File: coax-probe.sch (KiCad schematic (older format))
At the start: 28 parts, among them J1 Conn_01x02, J2 Conn_Coaxial, J3 Conn_01x02, J4 Conn_01x03, J5 Conn_Coaxial, J6 Conn_01x03, U1 THS3001, U2 INA128, U3 THS3001

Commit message: use dual-supply for differential amp buffer
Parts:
- added C8: 100nF, Capacitor_SMD:C_0402_1005Metric, symbol Device:C_Small
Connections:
- wire segments 86 -> 91
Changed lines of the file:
@@
 	6100 5450 5900 5450
-$Comp
-L power:GND #PWR010
-U 1 1 606A7C58
-P 5650 5050
-F 0 "#PWR010" H 5650 4800 50  0001 C CNN
-F 1 "GND" H 5650 4900 50  0000 C CNN
-F 2 "" H 5650 5050 50  0001 C CNN
-F 3 "" H 5650 5050 50  0001 C CNN
-	1    5650 5050
-	1    0    0    -1
-$EndComp
 $Comp
 L power:VCC #PWR09
@@
 	1    0    0    -1
 $EndComp
+$Comp
+L power:VSS #PWR010
+U 1 1 6077A074
+P 6300 5350
+F 0 "#PWR010" H 6300 5200 50  0001 C CNN
+F 1 "VSS" H 6300 5500 50  0000 C CNN
+F 2 "" H 6300 5350 50  0001 C CNN
+F 3 "" H 6300 5350 50  0001 C CNN
+	1    6300 5350
+	-1   0    0    1
+$EndComp
+$Comp
+L power:GND #PWR018
+U 1 1 6077A07A
+P 6500 5350
+F 0 "#PWR018" H 6500 5100 50  0001 C CNN
+F 1 "GND" H 6500 5200 50  0000 C CNN
+F 2 "" H 6500 5350 50  0001 C CNN
+F 3 "" H 6500 5350 50  0001 C CNN
+	1    6500 5350
+	1    0    0    -1
+$EndComp
+Wire Wire Line
+	6500 5150 6500 5100
+Wire Wire Line
+	6500 5100 6300 5100
+$Comp
+L Device:C_Small C8
+U 1 1 6077A082
+P 6500 5250
+F 0 "C8" H 6592 5296 50  0000 L CNN
+F 1 "100nF" H 6592 5205 50  0000 L CNN
+F 2 "Capacitor_SMD:C_0402_1005Metric" H 6538 5100 50  0001 C CNN
+F 3 "~" H 6500 5250 50  0001 C CNN
+	1    6500 5250
+	1    0    0    -1
+$EndComp
+Wire Wire Line
+	6300 5350 6300 5100
+Wire Wire Line
+	5650 5050 5650 5100
+Wire Wire Line
+	5650 5100 6300 5100
+Connection ~ 6300 5100
 $EndSCHEMATC

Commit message: Improvements, layout
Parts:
- removed C2, C7: 10uF, Capacitor_SMD:C_0603_1608Metric, symbol Device:C
- removed C4, C8: 100nF, Capacitor_SMD:C_0402_1005Metric, symbol Device:C_Small
- removed D1, D2: SM4007PL, Diode_SMD:D_SOD-123F, symbol Device:D_ALT
- removed J3: Conn_01x02, Connector_PinHeader_2.54mm:PinHeader_1x02_P2.54mm_Vertical, symbol Connector_Generic:Conn_01x02
- removed U1, U3: THS3001, Package_SO:SOIC-8_3.9x4.9mm_P1.27mm, symbol Amplifier_Operational:LMH6609MA
- added C10, C11: 10uF, Capacitor_SMD:C_0603_1608Metric, symbol Device:C
- added C13, C9: 100nF, Capacitor_SMD:C_0402_1005Metric, symbol Device:C_Small
- added J3: Conn_01x03, Connector_PinHeader_2.54mm:PinHeader_1x03_P2.54mm_Vertical, symbol Connector_Generic:Conn_01x03
- added R11: 0, Resistor_SMD:R_0603_1608Metric, symbol Device:R_US
- added R12: -, Resistor_SMD:R_0603_1608Metric, symbol Device:R_US
- added U1, U3: OPA690, Package_TO_SOT_SMD:TSOT-23-6, symbol Amplifier_Operational:LMH6611
- added U4: CJ431, Package_TO_SOT_SMD:SOT-23, symbol Reference_Voltage:CJ432
- J6: value Conn_01x03 -> Conn_01x02; footprint Connector_PinHeader_2.54mm:PinHeader_1x03_P2.54mm_Vertical -> Connector_PinHeader_2.54mm:PinHeader_1x02_P2.54mm_Vertical; symbol Connector_Generic:Conn_01x03 -> Connector_Generic:Conn_01x02
- R1: value 750 -> 175
- R2, R3, R8, R9: value 750 -> 402
- R5: value RG -> -
- R6: value 0 -> 175
- R7: value 10k -> 175
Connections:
- net labels added: REF
- net labels removed: Ref
- wire segments 91 -> 97
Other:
- note added: "1.2MHz Bandwidth G=0"
- note added: "175+25 balances 402||402\n\n175 ohm protects inputs up\nto 5V beyond rails."
- note added: "2.5V Vref shifts input into\nOPA690 common-mode range."
- note added: "2x gain compensates for\n50 ohm termination.\n220MHz Bandwidth (typ)"
- note added: "4.5V-36V"
- note added: "Common mode input range:\n-2V - VCC + 2V"
- note added: "Inputs protected to ±40V"
- note added: "±2.5V - ±6V"
- note added: "±3.3V common-mode input\nrange with ±5V supplies."
- note removed: "TODO: Check the art of electronics for input protection circuits"
- moved on the sheet: C3, C5, C6, J4, J5, R1, R10, R5, R8, R9, U2

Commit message: Add charge pump. Improve layout.
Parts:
- removed C11: 10uF, Capacitor_SMD:C_0603_1608Metric, symbol Device:C
- added C2, C4: 10uF, Capacitor_SMD:C_0805_2012Metric, symbol Device:C
- added C7: 100nF, Capacitor_SMD:C_0402_1005Metric, symbol Device:C_Small
- added JP1: LV, Jumper:SolderJumper-2_P1.3mm_Open_Pad1.0x1.5mm, symbol Jumper:SolderJumper_2_Open
- added U5: ICL7660, Package_SO:SOIC-8_3.9x4.9mm_P1.27mm, symbol Regulator_SwitchedCapacitor:ICL7660
- C1, C13, C3, C5, C9: LCSC (none) -> C1525; MPN (none) -> CL05B104KO5NNNC
- C10, C6: footprint Capacitor_SMD:C_0603_1608Metric -> Capacitor_SMD:C_0805_2012Metric; LCSC (none) -> C15850; MPN (none) -> CL21A106KAYNNNE
- J3: value Conn_01x03 -> Conn_01x02; footprint Connector_PinHeader_2.54mm:PinHeader_1x03_P2.54mm_Vertical -> Connector_PinHeader_2.54mm:PinHeader_1x02_P2.54mm_Vertical; symbol Connector_Generic:Conn_01x03 -> Connector_Generic:Conn_01x02
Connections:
- net GND: now also J3.2 (Pin_2), C2.1, C7.2, JP1.2 (B), U5.3 (GND); no longer J3.3 (Pin_3)
- net VCC: now also C7.1, U5.7 (OSC), U5.8 (V+)
- net VSS: now also C2.2, U5.5 (VOUT); no longer J3.2 (Pin_2)
- net OUT: now reaches J2.1 (In), R4.1
- net OUTD: now reaches J5.1 (In), R10.1
- new net: C4.1, U5.2 (CAP+)
- new net: C4.2, U5.4 (CAP-)
- new net: JP1.1 (A), U5.6 (LV)
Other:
- note added: "2.5V - 6V"
- note added: "5V-12V"
- note added: "Common mode input range:\n-2V - VCC+2V"
- note removed: "4.5V-36V"
- note removed: "Common mode input range:\n-2V - VCC + 2V"
- note removed: "±2.5V - ±6V"
- moved on the sheet: C1, C10, C5, C6, C9, J1, J2, J6, R1, R10, R2, R3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

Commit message: Fix 50-ohm trace width
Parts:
- J2, J5: value Conn_Coaxial -> SMA; footprint Beck:Coax_Cable_Solder -> Connector_Coaxial:SMA_Amphenol_132289_EdgeMount
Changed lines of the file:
@@
 P 5650 2000
 F 0 "J2" H 5750 1975 50  0000 L CNN
-F 1 "Conn_Coaxial" H 5750 1884 50  0000 L CNN
-F 2 "Beck:Coax_Cable_Solder" H 5650 2000 50  0001 C CNN
+F 1 "SMA" H 5750 1884 50  0000 L CNN
+F 2 "Connector_Coaxial:SMA_Amphenol_132289_EdgeMount" H 5650 2000 50  0001 C CNN
 F 3 " ~" H 5650 2000 50  0001 C CNN
 	1    5650 2000
@@
 P 6550 5150
 F 0 "J5" H 6650 5125 50  0000 L CNN
-F 1 "Conn_Coaxial" H 6650 5034 50  0000 L CNN
-F 2 "Beck:Coax_Cable_Solder" H 6550 5150 50  0001 C CNN
+F 1 "SMA" H 6650 5034 50  0000 L CNN
+F 2 "Connector_Coaxial:SMA_Amphenol_132289_EdgeMount" H 6550 5150 50  0001 C CNN
 F 3 " ~" H 6550 5150 50  0001 C CNN
 	1    6550 5150

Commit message: Use SMA connectors
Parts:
- removed JP1: LV, Jumper:SolderJumper-2_P1.3mm_Open_Pad1.0x1.5mm, symbol Jumper:SolderJumper_2_Open
- J3, J6: footprint Connector_PinHeader_2.54mm:PinHeader_1x02_P2.54mm_Vertical -> Connector_PinHeader_2.54mm:PinHeader_1x02_P2.54mm_Horizontal
- R12: value - -> DNP
- R5: value - -> DNP; footprint Capacitor_SMD:C_0603_1608Metric_Pad1.05x0.95mm_HandSolder -> Resistor_SMD:R_0603_1608Metric_Pad0.98x0.95mm_HandSolder
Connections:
- net GND: now also J3.1 (Pin_1), J4.1 (Pin_1), J6.1 (Pin_1); no longer J3.2 (Pin_2), J4.3 (Pin_3), J6.2 (Pin_2)
- net IN+: now also J4.2 (Pin_2); no longer J4.1 (Pin_1)
- net IN-: now also J4.3 (Pin_3); no longer J4.2 (Pin_2)
- net VCC: now also J3.2 (Pin_2), J6.2 (Pin_2); no longer J3.1 (Pin_1), J6.1 (Pin_1)
- no-connect marks 0 -> 1
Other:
- note added: "3V - 6V"
- note removed: "2.5V - 6V"
- moved on the sheet: J3
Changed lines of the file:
@@
 P 2900 5050
 F 0 "R5" H 2832 5004 50  0000 R CNN
-F 1 "-" H 2832 5095 50  0000 R CNN
-F 2 "Capacitor_SMD:C_0603_1608Metric_Pad1.05x0.95mm_HandSolder" H 2900 5050 50  0001 C CNN
+F 1 "DNP" H 2832 5095 50  0000 R CNN
+F 2 "Resistor_SMD:R_0603_1608Metric_Pad0.98x0.95mm_HandSolder" H 2900 5050 50  0001 C CNN
 F 3 "~" H 2900 5050 50  0001 C CNN
 	1    2900 5050
@@
 Wire Wire Line
 	3000 5150 2900 5150
-$Comp
-L Connector_Generic:Conn_01x03 J4
-U 1 1 606986ED
-P 2050 5100
-F 0 "J4" H 1968 5417 50  0000 C CNN
-F 1 "Conn_01x03" H 1968 5326 50  0000 C CNN
-F 2 "Connector_PinHeader_2.54mm:PinHeader_1x03_P2.54mm_Vertical" H 2050 5100 50  0001 C CNN
-F 3 "~" H 2050 5100 50  0001 C CNN
-	1    2050 5100
-	-1   0    0    -1
-$EndComp
 $Comp
 L power:GND #PWR01
@@
 L Connector_Generic:Conn_01x02 J6
 U 1 1 606D42E6
-P 10200 4950
-F 0 "J6" H 10280 4992 50  0000 L CNN
-F 1 "Conn_01x02" H 10280 4901 50  0000 L CNN
-F 2 "Connector_PinHeader_2.54mm:PinHeader_1x02_P2.54mm_Vertical" H 10200 4950 50  0001 C CNN
-F 3 "~" H 10200 4950 50  0001 C CNN
-	1    10200 4950
-	1    0    0    -1
+P 10200 5050
+F 0 "J6" H 10280 5092 50  0000 L CNN
+F 1 "Conn_01x02" H 10280 5001 50  0000 L CNN
+F 2 "Connector_PinHeader_2.54mm:PinHeader_1x02_P2.54mm_Horizontal" H 10200 5050 50  0001 C CNN
+F 3 "~" H 10200 5050 50  0001 C CNN
+	1    10200 5050
+	1    0    0    1
 $EndComp
 Text Label 2650 4850 0    50   ~ 0
@@
 $EndComp
 Wire Wire Line
-	10100 1950 10000 1950
-Wire Wire Line
 	9850 1850 9850 1800
 $Comp
 L Connector_Generic:Conn_01x02 J3
 U 1 1 6066DDD8
-P 10300 1950
-F 0 "J3" H 10380 1992 50  0000 L CNN
-F 1 "Conn_01x02" H 10380 1901 50  0000 L CNN
-F 2 "Connector_PinHeader_2.54mm:PinHeader_1x02_P2.54mm_Vertical" H 10300 1950 50  0001 C CNN
-F 3 "~" H 10300 1950 50  0001 C CNN
-	1    10300 1950
-	1    0    0    -1
+P 10200 2050
+F 0 "J3" H 10280 2092 50  0000 L CNN
+F 1 "Conn_01x02" H 10280 2001 50  0000 L CNN
+F 2 "Connector_PinHeader_2.54mm:PinHeader_1x02_P2.54mm_Horizontal" H 10200 2050 50  0001 C CNN
+F 3 "~" H 10200 2050 50  0001 C CNN
+	1    10200 2050
+	1    0    0    1
 $EndComp
 $Comp
@@
 P 7800 5400
 F 0 "R12" H 7868 5446 50  0000 L CNN
-F 1 "-" H 7868 5355 50  0000 L CNN
+F 1 "DNP" H 7868 5355 50  0000 L CNN
 F 2 "Resistor_SMD:R_0603_1608Metric" H 7800 5400 50  0001 C CNN
 F 3 "~" H 7800 5400 50  0001 C CNN
@@
 175+25 balances 402||402\n\n175 ohm protects inputs up\nto 5V beyond rails.
 Text Notes 10250 1800 0    50   ~ 0
-2.5V - 6V
+3V - 6V
 Text Notes 1300 2000 0    50   ~ 0
 ±3.3V common-mode input\nrange with ±5V supplies.
@@
 Wire Wire Line
 	10000 2300 10000 2200
-Wire Wire Line
-	10000 2050 10100 2050
 $Comp
 L Amplifier_Operational:LMH6611 U1
@@
 Wire Wire Line
 	2300 5200 2250 5200
-Wire Wire Line
-	3000 5250 2600 5250
-Wire Wire Line
-	2600 5250 2600 5100
-Wire Wire Line
-	2600 5100 2250 5100
-Wire Wire Line
-	2600 5000 2600 4850
-Wire Wire Line
-	2250 5000 2600 5000
 $Comp
 L Regulator_SwitchedCapacitor:ICL7660 U5
@@
 Wire Wire Line
 	10000 2200 10000 2050
-$Comp
-L Jumper:SolderJumper_2_Open JP1
-U 1 1 606AD10A
-P 8300 2400
-F 0 "JP1" V 8254 2468 50  0000 L CNN
-F 1 "LV" V 8345 2468 50  0000 L CNN
-F 2 "Jumper:SolderJumper-2_P1.3mm_Open_Pad1.0x1.5mm" H 8300 2400 50  0001 C CNN
-F 3 "~" H 8300 2400 50  0001 C CNN
-	1    8300 2400
-	0    1    1    0
-$EndComp
-$Comp
-L power:GND #PWR06
-U 1 1 606ADCFF
-P 8300 2550
-F 0 "#PWR06" H 8300 2300 50  0001 C CNN
-F 1 "GND" H 8300 2400 50  0000 C CNN
-F 2 "" H 8300 2550 50  0001 C CNN
-F 3 "" H 8300 2550 50  0001 C CNN
-	1    8300 2550
-	1    0    0    -1
-$EndComp
-Wire Wire Line
-	8300 2250 8300 2200
-Wire Wire Line
-	8300 2200 8250 2200
 Wire Wire Line
 	8250 2000 8300 2000
@@
 Text Label 5950 5150 0    50   ~ 0
 OUTD
+$Comp
+L Connector_Generic:Conn_01x03 J4
+U 1 1 606986ED
+P 2050 5100
+F 0 "J4" H 2050 4800 50  0000 C CNN
+F 1 "Conn_01x03" H 2050 4900 50  0000 C CNN
+F 2 "Connector_PinHeader_2.54mm:PinHeader_1x03_P2.54mm_Vertical" H 2050 5100 50  0001 C CNN
+F 3 "~" H 2050 5100 50  0001 C CNN
+	1    2050 5100
+	-1   0    0    1
+$EndComp
+Wire Wire Line
+	2250 5100 2600 5100
+Wire Wire Line
+	2600 5100 2600 4850
+Wire Wire Line
+	2550 5250 2550 5000
+Wire Wire Line
+	2550 5000 2250 5000
+Wire Wire Line
+	2550 5250 3000 5250
+NoConn ~ 8250 2200
 $EndSCHEMATC

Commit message: Add fab outputs and part numbers
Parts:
- R1, R6, R7: LCSC (none) -> C22828
- R10, R4: LCSC (none) -> C23185
- R11: LCSC (none) -> C21189
- R2, R3, R8, R9: LCSC (none) -> C23049
- U2: LCSC (none) -> C22233

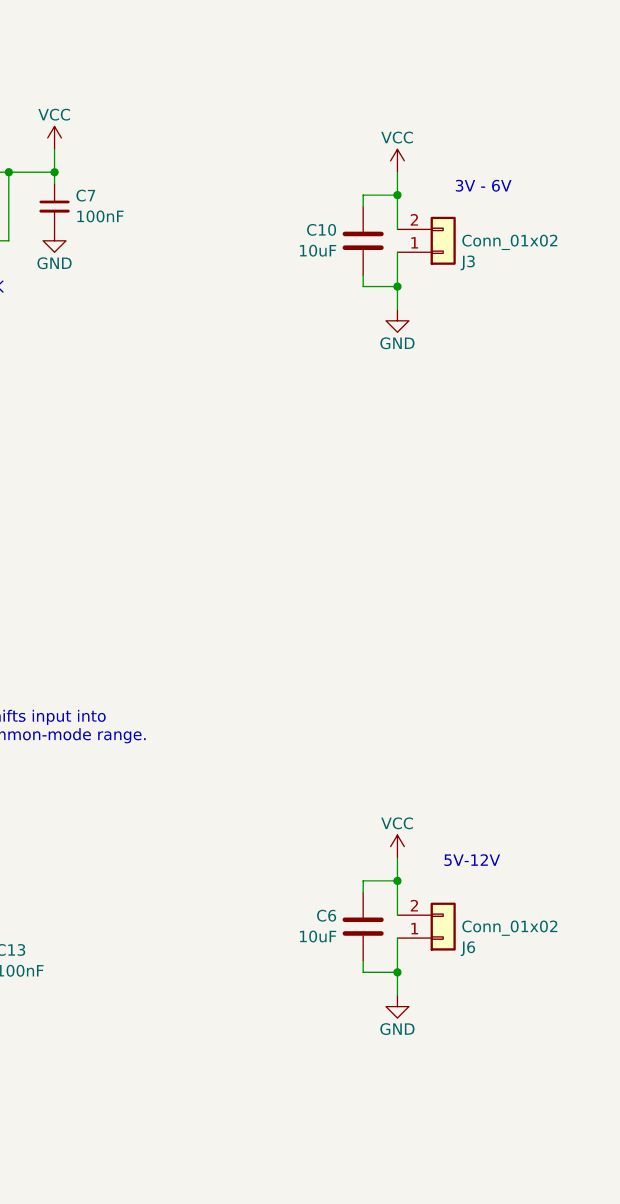
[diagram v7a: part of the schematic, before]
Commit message: Add power reverse-polarity protection
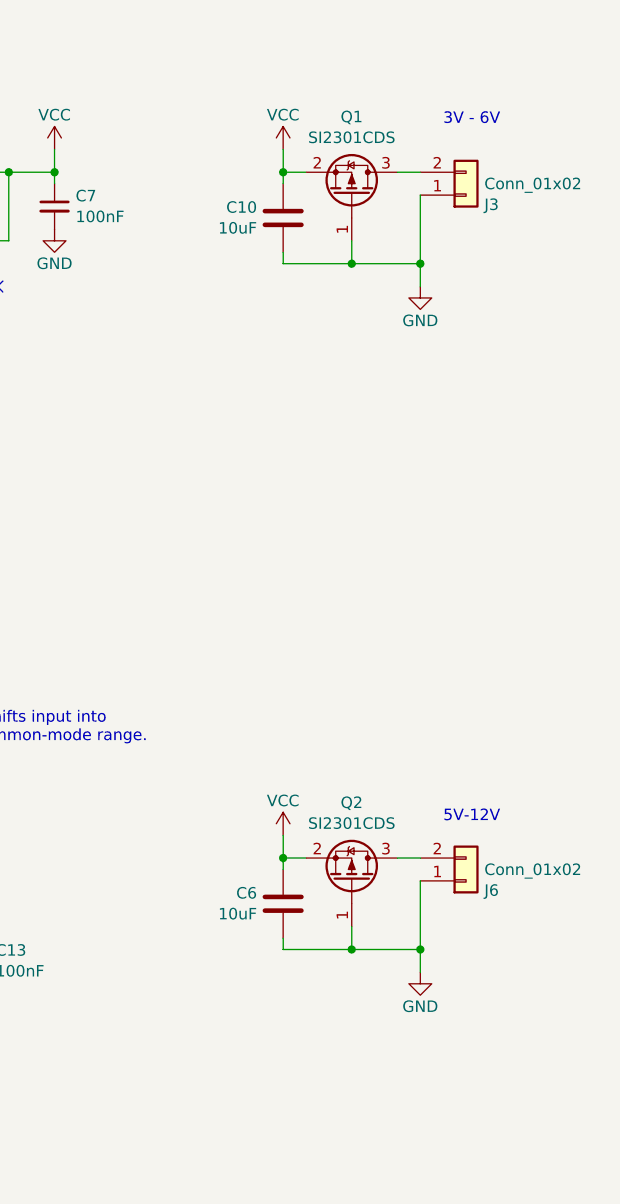
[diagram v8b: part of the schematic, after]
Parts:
- added Q1, Q2: SI2301CDS, Package_TO_SOT_SMD:SOT-23, symbol Transistor_FET:Si2371EDS
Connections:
- net GND: now also Q1.1 (G), Q2.1 (G)
- net VCC: now also Q1.2 (S), Q2.2 (S); no longer J3.2 (Pin_2), J6.2 (Pin_2)
- new net: J3.2 (Pin_2), Q1.3 (D)
- new net: J6.2 (Pin_2), Q2.3 (D)
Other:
- moved on the sheet: C10, C6, J3, J6
